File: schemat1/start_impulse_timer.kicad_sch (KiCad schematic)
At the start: 23 parts, among them Q1 BC547, Q2 BC547, Q3 BC547, Q4 BC547, U2 74LS390, U5 NE555P

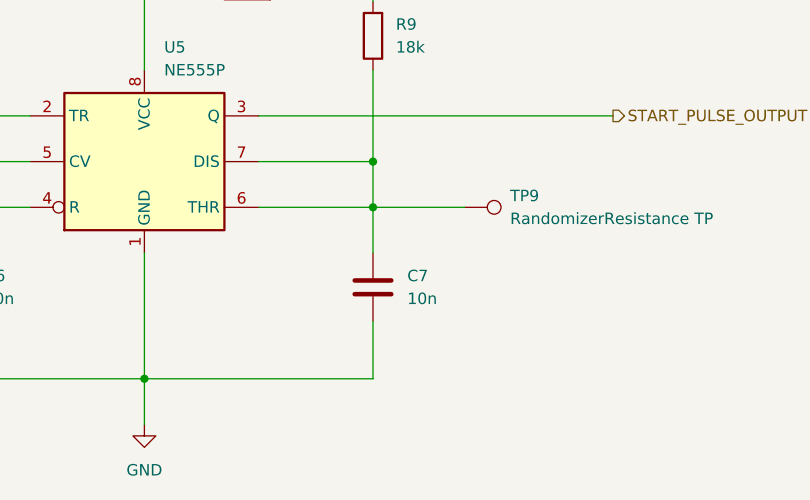
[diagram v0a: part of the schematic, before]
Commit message: zmiana elementu C7 na elektrolityczny, aktualizacja w schemacie i na pcb
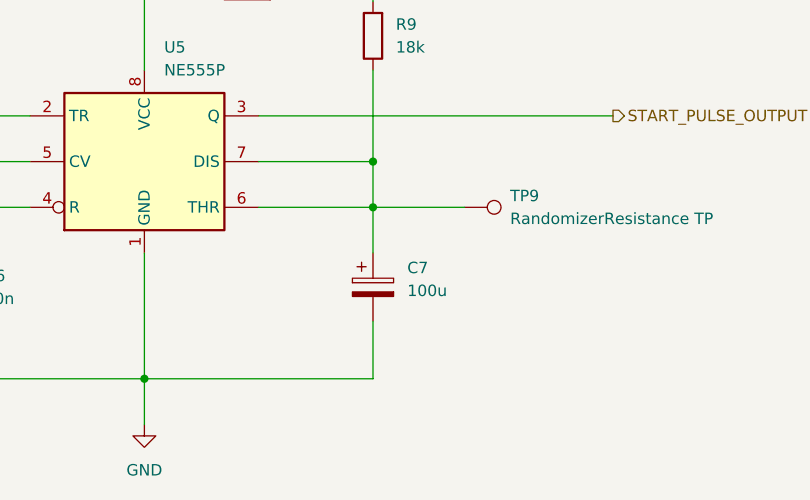
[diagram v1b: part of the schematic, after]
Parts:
- removed C7: 10n, Capacitor_THT:C_Disc_D3.4mm_W2.1mm_P2.50mm, symbol Device:C
- added C7: 100u, Capacitor_THT:CP_Radial_D6.3mm_P2.50mm, symbol Device:C_Polarized
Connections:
- net GND: now also C7.2
- net at R9.1, TP9.1, U5.6 (THR)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: now also C7.1
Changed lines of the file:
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@@
 	)
 	(symbol
-		(lib_id "Device:C")
+		(lib_id "Device:C_Polarized")
 		(at 152.4 133.35 0)
 		(unit 1)
@@
 		(fields_autoplaced yes)
 		(property "Reference" "C7"
-			(at 156.21 132.0799 0)
+			(at 156.21 131.1909 0)
 			(effects
 				(font
@@
 			)
 		)
-		(property "Value" "10n"
-			(at 156.21 134.6199 0)
+		(property "Value" "100u"
+			(at 156.21 133.7309 0)
 			(effects
 				(font
@@
 			)
 		)
-		(property "Footprint" "Capacitor_THT:C_Disc_D3.4mm_W2.1mm_P2.50mm"
+		(property "Footprint" "Capacitor_THT:CP_Radial_D6.3mm_P2.50mm"
 			(at 153.3652 137.16 0)
+			(show_name yes)
 			(effects
 				(font
@@
 			)
 		)
-		(property "Description" "Unpolarized capacitor"
+		(property "Description" "Polarized capacitor"
 			(at 152.4 133.35 0)
 			(effects
@@
 		)
 		(instances
-			(project "schemat"
+			(project ""
 				(path "/c9557d4c-8a19-4b35-91ba-3dde1f3d9070/46cb7a67-ecef-4b6e-ab38-56f9d8408944/a736c879-62d7-4fed-9573-699a1e1e2d1a"
 					(reference "C7")
